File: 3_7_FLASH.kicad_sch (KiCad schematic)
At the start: 3 parts, among them U1101 THD-2528-11SD-GF

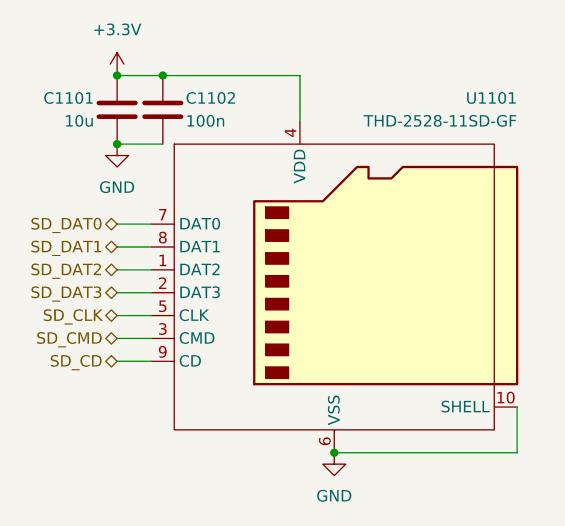
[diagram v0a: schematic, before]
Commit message: Finished restructuring schematic
Most components that were on page 3 are now in their own page
Added high-frequency 4.7 uF capacitor to servo power line
Continuity sensing on pyrochannels is multiplexed to one ADC on NAV.
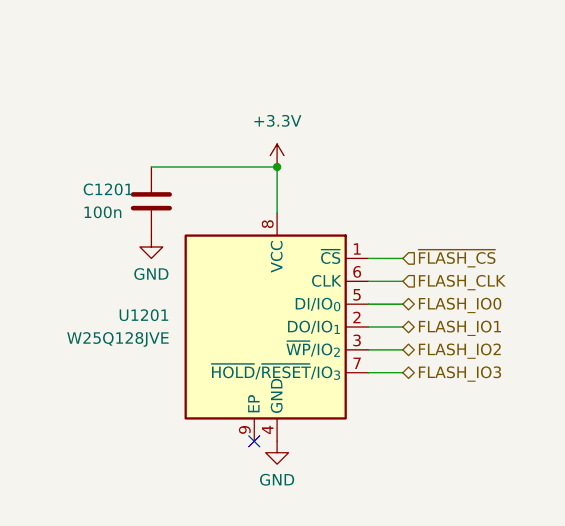
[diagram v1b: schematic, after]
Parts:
- removed C1101: 10u, Capacitor_SMD:C_0805_2012Metric, symbol Device:C
- removed C1102: 100n, Capacitor_SMD:C_0603_1608Metric, symbol Device:C
- removed U1101: THD-2528-11SD-GF, Polaris:TF-SMD_THD2528-11SD-GF, symbol Polaris_symbols:MicroSD_THD2528-11SD-GF
- added C1201: 100n, Capacitor_SMD:C_0603_1608Metric, symbol Device:C
- added U1201: W25Q128JVE, Package_SON:WSON-8-1EP_8x6mm_P1.27mm_EP3.4x4.3mm, symbol Memory_Flash:W25Q128JVE
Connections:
- net +3.3V: now also C1201.1, U1201.8 (VCC)
- net GND: now also C1201.2, U1201.4 (GND)
- new net FLASH_CLK: U1201.6 (CLK)
- new net FLASH_IO0: U1201.5 (DI/IO_{0})
- new net FLASH_IO1: U1201.2 (DO/IO_{1})
- new net FLASH_IO2: U1201.3 (~{WP}/IO_{2})
- new net FLASH_IO3: U1201.7 (~{HOLD}/~{RESET}/IO_{3})
- new net ~{FLASH_CS}: U1201.1 (~{CS})
- no-connect marks 0 -> 1

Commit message: Completed rough component placement
Began laying out traces
Small change to page 12 of schematic (FLASH):
Connected exposed pad to GND (not sure why I didn't connect it previously)
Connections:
- net GND: now also U1201.9 (EP)
- no-connect marks 1 -> 0
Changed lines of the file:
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@@
 	(paper "A4")
+	(junction
+		(at 144.78 120.65)
+		(diameter 0)
+		(color 0 0 0 0)
+	)
 	(junction
 		(at 144.78 90.17)
 		(diameter 0)
 		(color 0 0 0 0)
-	)
-	(no_connect
-		(at 142.24 120.65)
 	)
 	(wire
@@
 		)
 		(stroke
+			(width 0)
+			(type default)
+		)
+	)
+	(wire
+		(pts
+			(xy 142.24 120.65) (xy 144.78 120.65)
+		)
+		(stroke
